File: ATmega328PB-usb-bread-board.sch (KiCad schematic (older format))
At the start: 28 parts, among them J1 Conn_01x17, J2 Conn_01x17, J3 USB_B_Micro, J4 AVR-ISP-6, J5 Grove-I2C-connector, J6 Grove-I2C-connector, J7 Grove-I2C-connector, U1 ATmega328PB-MU, U2 CP2102N-A01-GQFN28, U3 LMV358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

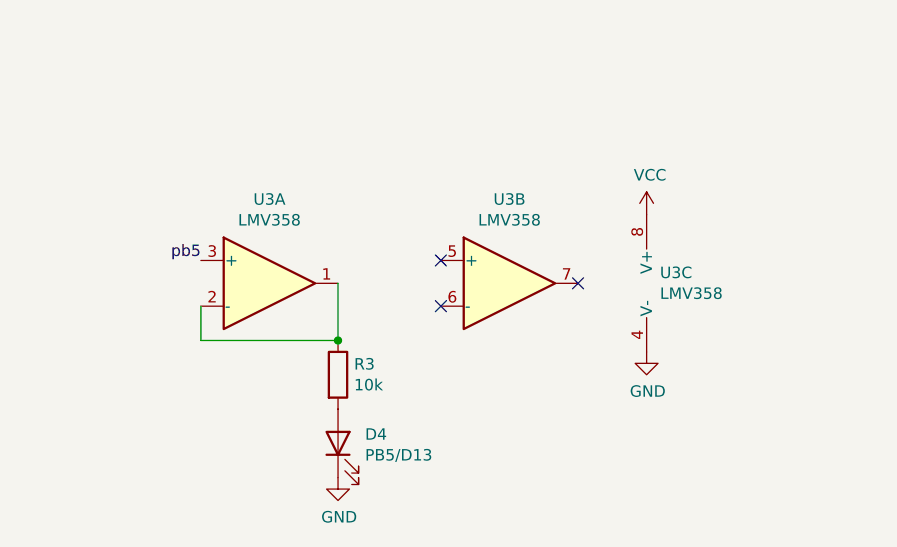
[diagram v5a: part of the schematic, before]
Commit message: Remove amplifier
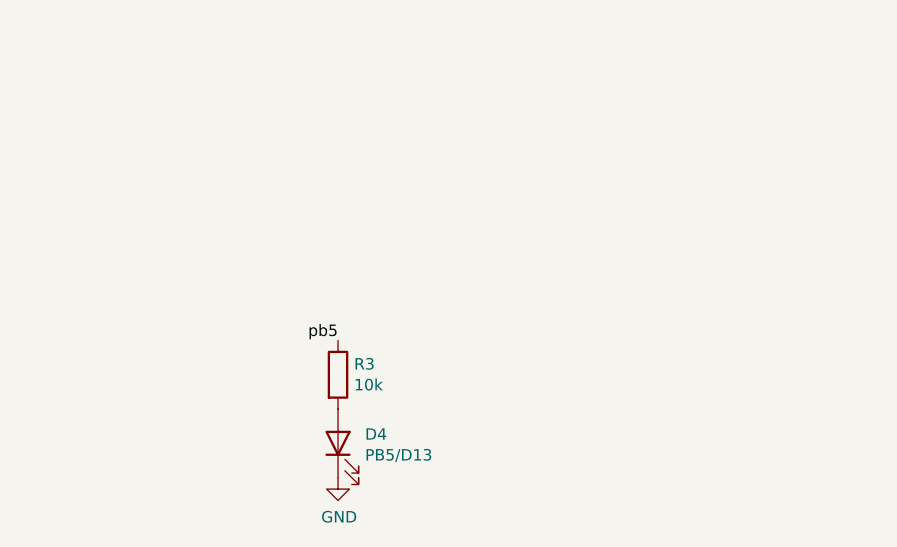
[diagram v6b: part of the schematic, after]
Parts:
- removed U3: LMV358, Package_SO:VSSOP-8_3.0x3.0mm_P0.65mm, symbol Amplifier_Operational:LMV358
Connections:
- net pb5: now also R3.1
- no-connect marks 23 -> 20
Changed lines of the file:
@@
 NoConn ~ 3450 2050
 NoConn ~ 3450 2350
-$Comp
-L Amplifier_Operational:LMV358 U3
-U 1 1 5F7FBC8F
-P 4400 6200
-F 0 "U3" H 4400 6567 50  0000 C CNN
-F 1 "LMV358" H 4400 6476 50  0000 C CNN
-F 2 "Package_SO:VSSOP-8_3.0x3.0mm_P0.65mm" H 4400 6200 50  0001 C CNN
-F 3 "http://www.ti.com/lit/ds/symlink/lmv324.pdf" H 4400 6200 50  0001 C CNN
-	1    4400 6200
-	1    0    0    -1
-$EndComp
-$Comp
-L Amplifier_Operational:LMV358 U3
-U 3 1 5F8010CF
-P 6150 6200
-F 0 "U3" H 6108 6246 50  0000 L CNN
-F 1 "LMV358" H 6108 6155 50  0000 L CNN
-F 2 "Package_SO:VSSOP-8_3.0x3.0mm_P0.65mm" H 6150 6200 50  0001 C CNN
-F 3 "http://www.ti.com/lit/ds/symlink/lmv324.pdf" H 6150 6200 50  0001 C CNN
-	3    6150 6200
-	1    0    0    -1
-$EndComp
-$Comp
-L Amplifier_Operational:LMV358 U3
-U 2 1 5F8029B5
-P 5450 6200
-F 0 "U3" H 5450 6567 50  0000 C CNN
-F 1 "LMV358" H 5450 6476 50  0000 C CNN
-F 2 "Package_SO:VSSOP-8_3.0x3.0mm_P0.65mm" H 5450 6200 50  0001 C CNN
-F 3 "http://www.ti.com/lit/ds/symlink/lmv324.pdf" H 5450 6200 50  0001 C CNN
-	2    5450 6200
-	1    0    0    -1
-$EndComp
-NoConn ~ 5750 6200
-NoConn ~ 5150 6100
-NoConn ~ 5150 6300
-$Comp
-L power:GND #PWR0120
-U 1 1 5F80F773
-P 6050 6500
-F 0 "#PWR0120" H 6050 6250 50  0001 C CNN
-F 1 "GND" H 6055 6327 50  0000 C CNN
-F 2 "" H 6050 6500 50  0001 C CNN
-F 3 "" H 6050 6500 50  0001 C CNN
-	1    6050 6500
-	1    0    0    -1
-$EndComp
-$Comp
-L power:VCC #PWR0121
-U 1 1 5F80FD8C
-P 6050 5900
-F 0 "#PWR0121" H 6050 5750 50  0001 C CNN
-F 1 "VCC" H 6065 6073 50  0000 C CNN
-F 2 "" H 6050 5900 50  0001 C CNN
-F 3 "" H 6050 5900 50  0001 C CNN
-	1    6050 5900
-	1    0    0    -1
-$EndComp
-Text Label 4100 6100 2    50   ~ 0
+Text Label 4700 6450 2    50   ~ 0
 pb5
-$Comp
-L Device:R R3
-U 1 1 5F81DA18
-P 4700 6600
-F 0 "R3" H 4770 6646 50  0000 L CNN
-F 1 "10k" H 4770 6555 50  0000 L CNN
-F 2 "Resistor_SMD:R_0603_1608Metric" V 4630 6600 50  0001 C CNN
-F 3 "~" H 4700 6600 50  0001 C CNN
-	1    4700 6600
-	1    0    0    -1
-$EndComp
 $Comp
 L Device:LED D4
@@
 	1    0    0    -1
 $EndComp
-Wire Wire Line
-	4100 6300 4100 6450
-Wire Wire Line
-	4100 6450 4700 6450
-Wire Wire Line
-	4700 6450 4700 6200
-Connection ~ 4700 6450
 $Comp
 L power:+3V3 #PWR0126
@@
 	1    0    0    -1
 $EndComp
+$Comp
+L Device:R R3
+U 1 1 5F81DA18
+P 4700 6600
+F 0 "R3" H 4770 6646 50  0000 L CNN
+F 1 "10k" H 4770 6555 50  0000 L CNN
+F 2 "Resistor_SMD:R_0603_1608Metric" V 4630 6600 50  0001 C CNN
+F 3 "~" H 4700 6600 50  0001 C CNN
+	1    4700 6600
+	1    0    0    -1
+$EndComp

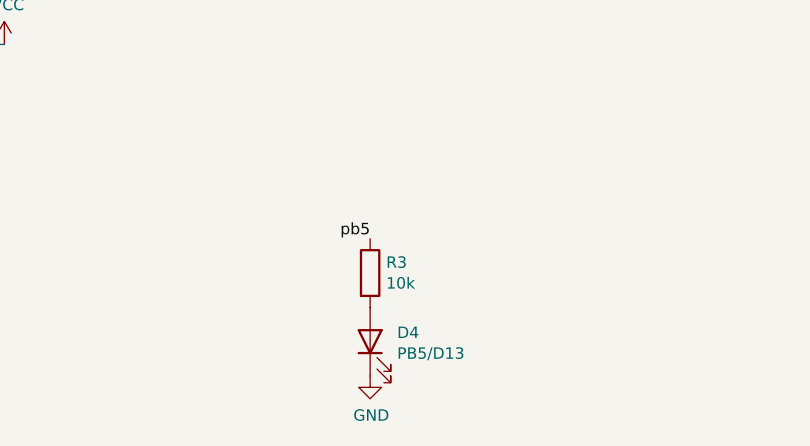
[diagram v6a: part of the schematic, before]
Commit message: Update a list of components and update label for resistors
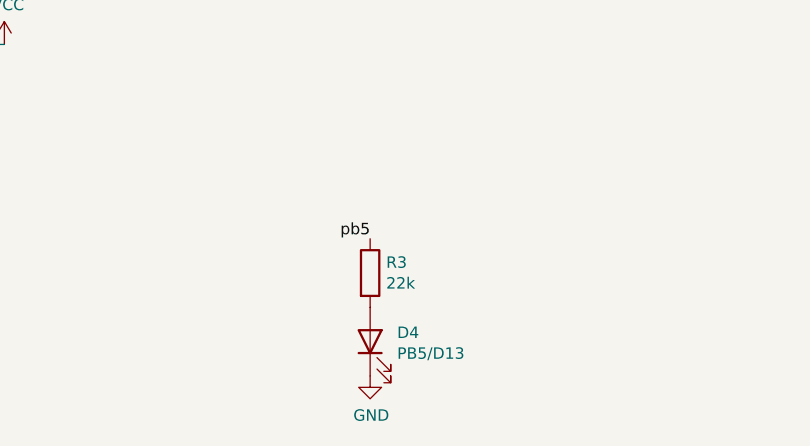
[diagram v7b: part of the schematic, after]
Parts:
- R3: value 10k -> 22k
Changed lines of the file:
@@
 P 4700 6600
 F 0 "R3" H 4770 6646 50  0000 L CNN
-F 1 "10k" H 4770 6555 50  0000 L CNN
+F 1 "22k" H 4770 6555 50  0000 L CNN
 F 2 "Resistor_SMD:R_0603_1608Metric" V 4630 6600 50  0001 C CNN
 F 3 "~" H 4700 6600 50  0001 C CNN

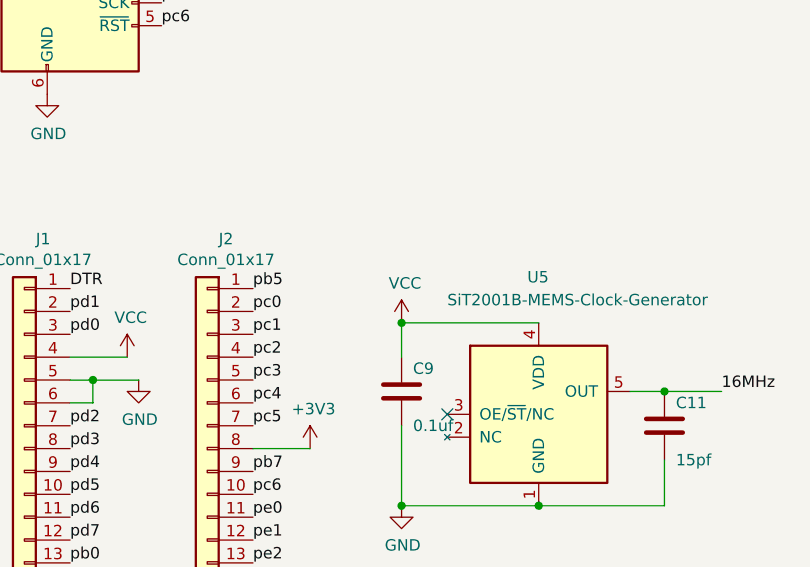
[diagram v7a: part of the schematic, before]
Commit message: Supply 3V3 for mems
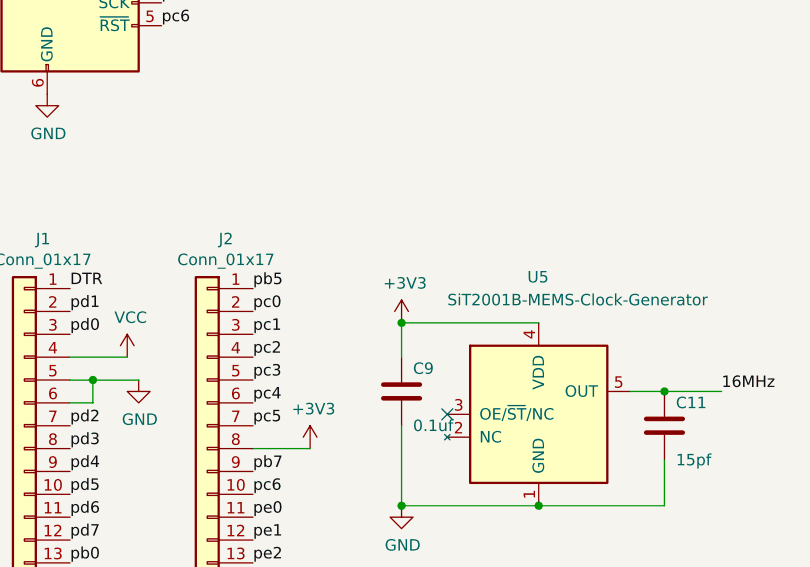
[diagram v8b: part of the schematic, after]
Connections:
- net +3V3: now also C9.1, U5.4 (VDD)
- net VCC: no longer C9.1, U5.4 (VDD)
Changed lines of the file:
@@
-$EndComp
-$Comp
-L power:VCC #PWR0127
-U 1 1 5F8E86D4
-P 9400 2950
-F 0 "#PWR0127" H 9400 2800 50  0001 C CNN
-F 1 "VCC" H 9415 3123 50  0000 C CNN
-F 2 "" H 9400 2950 50  0001 C CNN
-F 3 "" H 9400 2950 50  0001 C CNN
-	1    9400 2950
-	1    0    0    -1
 $EndComp
 $Comp
@@
 Wire Wire Line
 	9400 3100 9400 2950
-Connection ~ 9400 2950
 Wire Wire Line
 	10000 3750 9400 3750
@@
 	1    0    0    -1
 $EndComp
+$Comp
+L power:+3V3 #PWR?
+U 1 1 60A1FEB1
+P 9400 2950
+F 0 "#PWR?" H 9400 2800 50  0001 C CNN
+F 1 "+3V3" H 9415 3123 50  0000 C CNN
+F 2 "" H 9400 2950 50  0001 C CNN
+F 3 "" H 9400 2950 50  0001 C CNN
+	1    9400 2950
+	1    0    0    -1
+$EndComp
+Connection ~ 9400 2950
 $EndSCHEMATC
